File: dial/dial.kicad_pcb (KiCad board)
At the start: 2 copper layers, 36 x 36 mm, 65 parts, among them U1 MAX6951

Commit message: add components
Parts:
- added BT1: Battery_Cell, Custom Footprints:3008_coin_cell, B.Cu at (144.0, 60.6)
- added C1: C_Small, Capacitor_SMD:C_0402_1005Metric, F.Cu at (171.7, 57.5)
- added C2: C_Small, Capacitor_SMD:C_0402_1005Metric, F.Cu at (174.6, 57.5)
- added C3: C_Small, Capacitor_SMD:C_0402_1005Metric, F.Cu at (177.5, 57.5)
- added C4: C_Small, Capacitor_SMD:C_0402_1005Metric, F.Cu at (180.4, 57.5)
- added C5: C_Small, Capacitor_SMD:C_0402_1005Metric, F.Cu at (183.3, 57.5)
- added SW1: SW_Push, Button_Switch_SMD:Panasonic_EVQPUK_EVQPUB, B.Cu at (166.0, 50.1)
- added SW2: SW_Push, Button_Switch_SMD:Panasonic_EVQPUK_EVQPUB, B.Cu at (163.5, 41.9)
- added SW3: SW_Push, Button_Switch_SMD:Panasonic_EVQPUK_EVQPUB, F.Cu at (198.6, 56.0)
- added U2: ATSAMD10C14A-SS, Package_SO:SOIC-14_3.9x8.7mm_P1.27mm, B.Cu at (159.5, 50.0)
- added U3: BMA250E, Package_LGA:LGA-12_2x2mm_P0.5mm, F.Cu at (204.7, 48.7)
- added Y1: Crystal_Small, Crystal:Crystal_SMD_5032-2Pin_5.0x3.2mm, B.Cu at (160.2, 57.5)
- U1: moved to B.Cu
- moved U1 39.5 mm to (149.9, 64.3), turned to 180 degrees
- moved D51 24.1 mm to (153.4, 46.8), turned to 225 degrees
- moved D44 21.4 mm to (150.0, 45.5), turned to 270 degrees
- moved D37 20.6 mm to (146.6, 46.8)
- moved D30 13.9 mm to (148.3, 33.2), turned to 276 degrees
- moved D23 12.2 mm to (146.6, 33.5), turned to 282 degrees
- moved D52 10.7 mm to (140.1, 36.3), turned to 306 degrees
- moved D59 10.5 mm to (141.7, 35.3), turned to 300 degrees
- moved D16 10.2 mm to (144.9, 33.9), turned to 288 degrees
- moved D31 7.94 mm to (136.4, 40.1), turned to 324 degrees
- moved D24 7.72 mm to (135.4, 41.5), turned to 330 degrees
- moved D38 7.39 mm to (137.5, 38.7), turned to 318 degrees
- moved D9 7.24 mm to (143.3, 34.5), turned to 294 degrees
- moved D45 5.76 mm to (138.7, 37.4), turned to 312 degrees
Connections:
- U1 pad 1: (no net) -> Net-(U1-Pad1)
- U1 pad 15: (no net) -> Net-(U1-Pad15)
- U1 pad 16: (no net) -> Net-(U1-Pad16)
- U1 pad 2: (no net) -> Net-(U1-Pad2)
- U1 pad 7: (no net) -> Net-(U1-Pad7)
- U1 pad 8: (no net) -> Net-(U1-Pad8)
- U1 pad 9: (no net) -> Net-(U1-Pad9)
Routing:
- net Net-(Y1-Pad1): track 0.00 -> 144.4 mm
- net SEG8: track 87.9 -> 0.00 mm
- net Net-(Y1-Pad2): track 0.00 -> 87.9 mm
- net Net-(BT1-Pad1): track 0.00 -> 81.6 mm
- net DIG7: track 81.6 -> 5.43 mm
- net DIG6: track 75.4 -> 12.7 mm
- net DIG5: track 69.1 -> 12.9 mm
- net DIG4: track 62.8 -> 75.5 mm

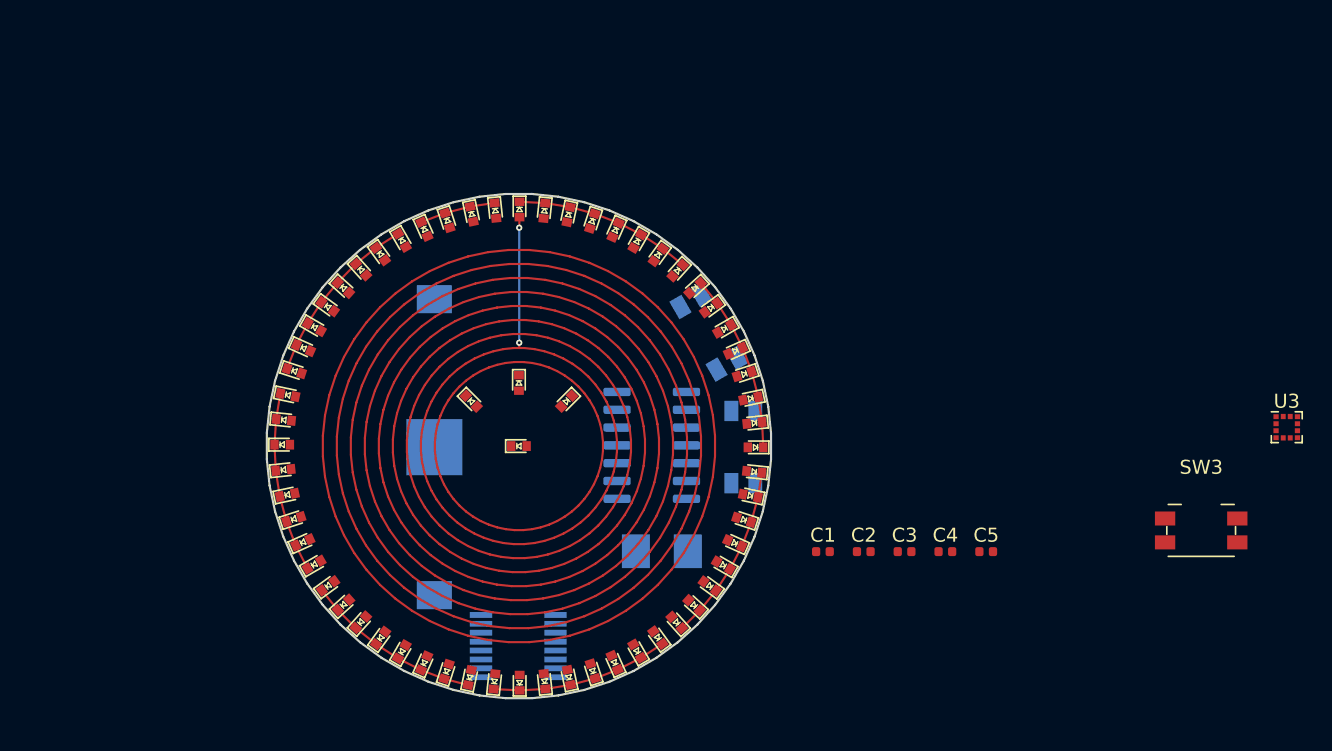
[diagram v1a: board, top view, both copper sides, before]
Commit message: rework for SAMD21
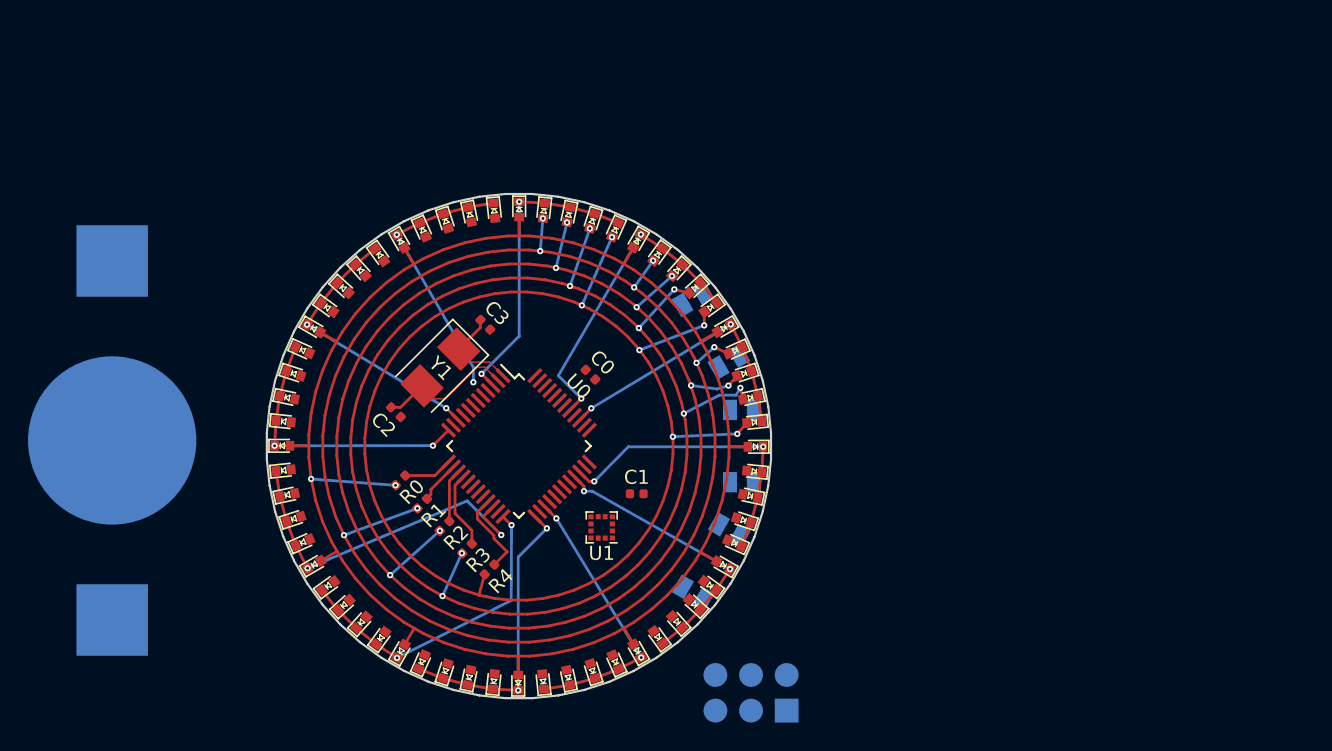
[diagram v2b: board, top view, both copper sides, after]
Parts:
- removed the C1 at (171.7, 57.5)
- removed the C2 at (174.6, 57.5)
- removed D60, D61, D62, D63, D64: LED_ALT, Custom Footprints:LED_0402-Clean-bar
- removed the U1 at (149.9, 64.3)
- removed U2: ATSAMD10C14A-SS, Package_SO:SOIC-14_3.9x8.7mm_P1.27mm
- added C0: 0.1uF, Capacitor_SMD:C_0402_1005Metric, F.Cu at (155.1, 44.9)
- added D0: LED_ALT, Custom Footprints:LED_0402-Clean, F.Cu at (150.0, 33.1)
- added J1: SWD-PROG-6, Custom Footprints:ISP_SMD, B.Cu at (169.1, 68.9)
- added R0: 220R, Resistor_SMD:R_0402_1005Metric, F.Cu at (141.6, 52.4)
- added R1: 220R, Resistor_SMD:R_0402_1005Metric, F.Cu at (143.1, 54.1)
- added R2: 220R, Resistor_SMD:R_0402_1005Metric, F.Cu at (144.7, 55.7)
- added R3: 220R, Resistor_SMD:R_0402_1005Metric, F.Cu at (146.3, 57.3)
- added R4: 220R, Resistor_SMD:R_0402_1005Metric, F.Cu at (147.9, 58.8)
- added U0: ATSAMD21G18A-AUT, Package_QFP:TQFP-48_7x7mm_P0.5mm, F.Cu at (150.0, 50.0)
- BT1: footprint Custom Footprints:3008_coin_cell -> Battery:BatteryHolder_Keystone_3002_1x2032
- C2: renamed from C4; value C_Small -> 12pF
- C3: value C_Small -> 12pF
- D1, D10, D11, D12, D13, D14, D15, D16, D17, D18, D19, D2, D20, D21, D22, D23, D24, D25, D26, D27, D28, D29, D3, D30, D31, D32, D33, D34, D35, D36, D37, D38, D39, D4, D40, D41, D42, D43, D44, D45, D46, D47, D48, D49, D5, D50, D51, D52, D53, D54, D55, D56, D57, D58, D59, D6, D7, D8, D9: footprint Custom Footprints:LED_0402-Clean-bar -> Custom Footprints:LED_0402-Clean
- SW1: value SW_Push -> UP
- SW2: value SW_Push -> OK
- SW3: value SW_Push -> DOWN; moved to B.Cu
- Y1: value Crystal_Small -> 32.768KHz; moved to F.Cu
- moved U1 49.4 mm to (155.9, 55.8), turned to 180 degrees
- moved C2 40.4 mm to (141.2, 47.6), turned to 315 degrees
- moved SW3 35.0 mm to (163.7, 58.2), turned to 60 degrees
- moved C3 34.0 mm to (147.6, 41.4), turned to 315 degrees
- moved D30 33.7 mm to (149.9, 66.9), turned to 90 degrees
- moved D43 33.7 mm to (133.5, 53.5), turned to 12 degrees
- moved D11 33.7 mm to (165.4, 43.2), turned to 204 degrees
- moved D17 33.6 mm to (166.5, 53.6), turned to 168 degrees
- moved D49 33.6 mm to (134.6, 43.2), turned to 336 degrees
- moved D56 33.0 mm to (143.1, 34.6), turned to 294 degrees
- moved D24 33.0 mm to (159.9, 63.6), turned to 126 degrees
- moved D55 32.6 mm to (141.6, 35.4), turned to 300 degrees
- moved D23 32.6 mm to (161.3, 62.5), turned to 132 degrees
- moved D36 32.5 mm to (140.2, 63.7), turned to 54 degrees
- moved D50 31.6 mm to (135.4, 41.6), turned to 330 degrees
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- renumbered C5 to C1, U3 to U1
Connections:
- BT1 pad 1: Net-(BT1-Pad1) -> +BATT
- BT1 pad 2: Net-(BT1-Pad2) -> GND
- C1 pad 1: Net-(C5-Pad1) -> +BATT
- C1 pad 2: Net-(C5-Pad2) -> GND
- C2 pad 1: Net-(C4-Pad1) -> XOUT
- C2 pad 2: Net-(C4-Pad2) -> GND
- C3 pad 1: Net-(C3-Pad1) -> XIN
- C3 pad 2: Net-(C3-Pad2) -> GND
- D1 pad 1: DIG0 -> TWELVE
- D1 pad 2: DIG1 -> M1
- D10 pad 1: DIG6 -> TWO
- D10 pad 2: DIG0 -> HOUR
- D11 pad 1: DIG5 -> TWO
- D11 pad 2: DIG0 -> M1
- D12 pad 1: DIG4 -> TWO
- D12 pad 2: DIG0 -> M2
- D13 pad 1: DIG3 -> TWO
- D13 pad 2: DIG0 -> M3
- D14 pad 1: DIG2 -> TWO
- D14 pad 2: DIG0 -> M4
- D15 pad 1: DIG1 -> THREE
- D15 pad 2: DIG0 -> HOUR
- D16 pad 1: DIG7 -> THREE
- D16 pad 2: DIG1 -> M1
- D17 pad 1: DIG6 -> THREE
- D17 pad 2: DIG1 -> M2
- D18 pad 1: DIG5 -> THREE
- D18 pad 2: DIG1 -> M3
- D19 pad 1: DIG4 -> THREE
- D19 pad 2: DIG1 -> M4
- D2 pad 1: DIG0 -> TWELVE
- D2 pad 2: DIG2 -> M2
- D20 pad 1: DIG3 -> FOUR
- D20 pad 2: DIG1 -> HOUR
- D21 pad 1: DIG2 -> FOUR
- D21 pad 2: DIG1 -> M1
- D22 pad 1: DIG1 -> FOUR
- D22 pad 2: DIG2 -> M2
- D23 pad 1: DIG7 -> FOUR
- D23 pad 2: DIG2 -> M3
- D24 pad 1: DIG6 -> FOUR
- D24 pad 2: DIG2 -> M4
- D25 pad 1: DIG5 -> FIVE
- D25 pad 2: DIG2 -> HOUR
- D26 pad 1: DIG4 -> FIVE
- D26 pad 2: DIG2 -> M1
- D27 pad 1: DIG3 -> FIVE
- D27 pad 2: DIG2 -> M2
- D28 pad 1: DIG2 -> FIVE
- D28 pad 2: DIG3 -> M3
- D29 pad 1: DIG1 -> FIVE
- D29 pad 2: DIG3 -> M4
- D3 pad 1: DIG0 -> TWELVE
- D3 pad 2: DIG3 -> M3
- D30 pad 1: DIG7 -> SIX
- D30 pad 2: DIG3 -> HOUR
- D31 pad 1: DIG6 -> SIX
- D31 pad 2: DIG3 -> M1
- D32 pad 1: DIG5 -> SIX
- D32 pad 2: DIG3 -> M2
- D33 pad 1: DIG4 -> SIX
- D33 pad 2: DIG3 -> M3
- D34 pad 1: DIG3 -> SIX
- D34 pad 2: DIG4 -> M4
- D35 pad 1: DIG2 -> SEVEN
- D35 pad 2: DIG4 -> HOUR
- D36 pad 1: DIG1 -> SEVEN
- D36 pad 2: DIG4 -> M1
- D37 pad 1: DIG7 -> SEVEN
- D37 pad 2: DIG4 -> M2
- D38 pad 1: DIG6 -> SEVEN
- D38 pad 2: DIG4 -> M3
- D39 pad 1: DIG5 -> SEVEN
- D39 pad 2: DIG4 -> M4
- D4 pad 1: DIG0 -> TWELVE
- D4 pad 2: DIG4 -> M4
- D40 pad 1: DIG4 -> EIGHT
- D40 pad 2: DIG5 -> HOUR
- D41 pad 1: DIG3 -> EIGHT
- D41 pad 2: DIG5 -> M1
- D42 pad 1: DIG2 -> EIGHT
- D42 pad 2: DIG5 -> M2
- D43 pad 1: DIG1 -> EIGHT
- D43 pad 2: DIG5 -> M3
- D44 pad 1: DIG7 -> EIGHT
- D44 pad 2: DIG5 -> M4
- D45 pad 1: DIG6 -> NINE
- D45 pad 2: DIG5 -> HOUR
- D46 pad 1: DIG5 -> NINE
- D46 pad 2: DIG6 -> M1
- D47 pad 1: DIG4 -> NINE
- D47 pad 2: DIG6 -> M2
- D48 pad 1: DIG3 -> NINE
- D48 pad 2: DIG6 -> M3
- D49 pad 1: DIG2 -> NINE
- D49 pad 2: DIG6 -> M4
- D5 pad 1: DIG0 -> ONE
- D5 pad 2: DIG5 -> HOUR
- D50 pad 1: DIG1 -> TEN
- D50 pad 2: DIG6 -> HOUR
- D51 pad 1: DIG7 -> TEN
- D51 pad 2: DIG6 -> M1
- D52 pad 1: DIG6 -> TEN
- D52 pad 2: DIG7 -> M2
- D53 pad 1: DIG5 -> TEN
- D53 pad 2: DIG7 -> M3
- D54 pad 1: DIG4 -> TEN
- D54 pad 2: DIG7 -> M4
- D55 pad 1: DIG3 -> ELEVEN
- D55 pad 2: DIG7 -> HOUR
- D56 pad 1: DIG2 -> ELEVEN
- D56 pad 2: DIG7 -> M1
- D57 pad 1: DIG1 -> ELEVEN
- D57 pad 2: DIG7 -> M2
- D58 pad 1: DIG7 -> ELEVEN
- D58 pad 2: SEG8 -> M3
- D59 pad 1: DIG6 -> ELEVEN
- D59 pad 2: SEG8 -> M4
- D6 pad 1: DIG0 -> ONE
- D6 pad 2: DIG6 -> M1
- D7 pad 1: DIG0 -> ONE
- D7 pad 2: DIG7 -> M2
- D8 pad 1: DIG0 -> ONE
- D8 pad 2: SEG8 -> M3
- D9 pad 1: DIG7 -> ONE
- D9 pad 2: DIG0 -> M4
- SW1 pad 1: Net-(SW1-Pad1) -> GND
- SW2 pad 1: Net-(SW2-Pad1) -> GND
- SW3 pad 1: Net-(SW3-Pad1) -> GND
- U1 pad 1: Net-(U3-Pad1) -> (no net)
- U1 pad 10: Net-(U3-Pad10) -> (no net)
- U1 pad 11: Net-(U3-Pad11) -> (no net)
- U1 pad 12: Net-(U3-Pad12) -> (no net)
- U1 pad 2: Net-(U3-Pad2) -> (no net)
- U1 pad 3: Net-(U3-Pad3) -> +BATT
- U1 pad 4: Net-(U3-Pad4) -> GND
- U1 pad 5: Net-(U3-Pad5) -> (no net)
- U1 pad 6: Net-(U3-Pad6) -> (no net)
- U1 pad 7: Net-(U3-Pad7) -> +BATT
- U1 pad 8: Net-(U3-Pad8) -> GND
- U1 pad 9: Net-(U3-Pad9) -> GND
- Y1 pad 1: Net-(Y1-Pad1) -> XIN
- Y1 pad 2: Net-(Y1-Pad2) -> XOUT
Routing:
- net Net-(Y1-Pad1): track 144.4 -> 0.00 mm
- net HOUR: track 0.00 -> 116.3 mm, vias 0 -> 2
- net M1: track 0.00 -> 101.0 mm, vias 0 -> 8
- net M2: track 0.00 -> 96.7 mm, vias 0 -> 8
- net M3: track 0.00 -> 93.4 mm, vias 0 -> 8
- net Net-(Y1-Pad2): track 87.9 -> 0.00 mm
- net M4: track 0.00 -> 87.5 mm, vias 0 -> 6
- net Net-(BT1-Pad1): track 81.6 -> 0.00 mm
- net DIG4: track 75.5 -> 0.00 mm
- net DIG3: track 69.3 -> 0.00 mm
- net DIG1: track 66.1 -> 0.00 mm, vias 2 -> 0
- net DIG2: track 63.0 -> 0.00 mm
- net DIG0: track 50.4 -> 0.00 mm
- net EIGHT: track 0.00 -> 26.0 mm, vias 0 -> 2
- net SEVEN: track 0.00 -> 22.6 mm, vias 0 -> 2
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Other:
- rule via_min_size: 0.2 -> 0.45

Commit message: Wire it up
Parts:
- moved J1 23.2 mm to (159.8, 47.6), turned to 180 degrees
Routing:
- net M4: track 87.5 -> 135.8 mm, vias 6 -> 24
- net M3: track 93.4 -> 132.5 mm, vias 8 -> 26
- net M2: track 96.7 -> 128.7 mm, vias 8 -> 25
- net M1: track 101.0 -> 122.4 mm, vias 8 -> 25
- net SWCLK: track 0.00 -> 9.78 mm, vias 0 -> 1
- net SWDIO: track 0.00 -> 9.21 mm, vias 0 -> 1
- net RESET: track 0.00 -> 9.05 mm, vias 0 -> 1

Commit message: Wired it all up
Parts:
- removed BT1: Battery_Cell, Battery:BatteryHolder_Keystone_3002_1x2032
- added C4: 1uF, Capacitor_SMD:C_0402_1005Metric, B.Cu at (150.8, 48.9)
- added C5: 1uF, Capacitor_SMD:C_0402_1005Metric, B.Cu at (147.4, 50.5)
- added C6: 1uF, Capacitor_SMD:C_0402_1005Metric, B.Cu at (142.9, 43.5)
- added C7: 4.7uF, Capacitor_SMD:C_0402_1005Metric, B.Cu at (147.4, 42.0)
- added C8: 4.7uF, Capacitor_SMD:C_0402_1005Metric, B.Cu at (151.7, 40.3)
- added J0: Battery Pads, Custom Footprints:150mAh-Lipo, B.Cu at (152.3, 47.0)
- added R5: 10M, Resistor_SMD:R_0402_1005Metric, B.Cu at (144.6, 44.3)
- added R6: 10M, Resistor_SMD:R_0402_1005Metric, B.Cu at (143.7, 45.2)
- added R7: 2K, Resistor_SMD:R_0402_1005Metric, B.Cu at (152.4, 42.4)
- added U2: Reg, Package_TO_SOT_SMD:SOT-23, B.Cu at (150.0, 51.3)
- added U3: CHG CTRL, Package_TO_SOT_SMD:SOT-23-5, B.Cu at (149.9, 43.0)
- C0: moved to B.Cu
- moved C0 5.72 mm to (153.5, 50.4), turned to 45 degrees
- moved C1 4.83 mm to (154.6, 56.4), turned to 270 degrees
- moved U1 0.78 mm to (156.5, 56.3), turned to 0 degrees
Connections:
- C0 pad 2: +BATT -> +3V3
- C1 pad 1: +BATT -> +3V3
- J1 pad 2: +BATT -> CHARGE
- U0 pad 17: +BATT -> +3V3
- U0 pad 28: (no net) -> SDx
- U0 pad 29: (no net) -> SDO
- U0 pad 30: (no net) -> SCx
- U0 pad 31: (no net) -> CSB
- U0 pad 36: +BATT -> +3V3
- U0 pad 43: +BATT -> +3V3
- U0 pad 44: +BATT -> +3V3
- U0 pad 6: +BATT -> +3V3
- U0 pad 8: (no net) -> BAT_MON
- U1 pad 1: (no net) -> SDO
- U1 pad 10: (no net) -> CSB
- U1 pad 11: (no net) -> GND
- U1 pad 12: (no net) -> SCx
- U1 pad 2: (no net) -> SDx
- U1 pad 3: +BATT -> +3V3
- U1 pad 5: (no net) -> GND
- U1 pad 6: (no net) -> GND
- U1 pad 7: +BATT -> +3V3
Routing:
- net GND: track 0.00 -> 105.4 mm, vias 0 -> 5
- net +3V3: track 0.00 -> 38.5 mm, vias 0 -> 3
- net CHARGE: track 0.00 -> 17.9 mm
- net Net-(SW3-Pad2): track 0.00 -> 16.8 mm, vias 0 -> 1
- net +BATT: track 0.00 -> 14.8 mm
- net Net-(SW1-Pad2): track 0.00 -> 13.1 mm, vias 0 -> 1
- net Net-(SW2-Pad2): track 0.00 -> 11.6 mm, vias 0 -> 1
- net BAT_MON: track 0.00 -> 7.15 mm, vias 0 -> 1
- net CSB: track 0.00 -> 5.27 mm
- net SDx: track 0.00 -> 4.63 mm
- net SCx: track 0.00 -> 4.47 mm
- net SDO: track 0.00 -> 4.00 mm
- net TWELVE: track 21.8 -> 23.5 mm
- net Net-(R7-Pad1): track 0.00 -> 1.55 mm
- net ELEVEN: track 19.3 -> 20.6 mm
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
